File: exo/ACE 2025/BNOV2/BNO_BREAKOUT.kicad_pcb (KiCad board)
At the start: 2 copper layers, 67.5 x 45 mm, 17 parts, among them J2 RJ45, SW1 SW_SPDT, U1 4754, U2 PCA9615DPZ, U3 AP7361C-33E

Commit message: BNOV2 V0.2
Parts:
- removed C4: 4.7uF, Capacitor_SMD:C_1812_4532Metric_Pad1.57x3.40mm_HandSolder
- removed D2: BAV99, Package_TO_SOT_SMD:SOT-23
- added REF**: MountingHole_3.2mm_M3, MountingHole:MountingHole_3.2mm_M3, F.Cu at (121.0, 71.5)
- added REF**: MountingHole_3.2mm_M3, MountingHole:MountingHole_3.2mm_M3, F.Cu at (157.0, 125.5)
- added REF**: MountingHole_3.2mm_M3, MountingHole:MountingHole_3.2mm_M3, F.Cu at (121.0, 125.5)
- added REF**: MountingHole_3.2mm_M3, MountingHole:MountingHole_3.2mm_M3, F.Cu at (157.0, 71.5)
- C2, C3: value 4.7uF -> 1n
- D4: value ESD9B3.3ST5G -> D_TVS_Filled; footprint Diode_SMD:D_SOD-923 -> Diode_SMD:D_0805_2012Metric
- moved J2 36.8 mm to (129.1, 114.0), turned to 0 degrees
- moved U3 36.1 mm to (146.7, 118.7), turned to -90 degrees
- moved SW1 33.9 mm to (129.5, 97.4), turned to -90 degrees
- moved C5 30.9 mm to (151.5, 111.5)
- moved D5 29.6 mm to (149.0, 111.4), turned to 90 degrees
- moved C6 26.1 mm to (144.0, 111.5), turned to 90 degrees
- moved D3 25.5 mm to (146.5, 94.4), turned to 90 degrees
- moved R1 23.7 mm to (146.5, 111.5)
- moved D1 23.6 mm to (139.5, 94.4), turned to 90 degrees
- moved U2 16.1 mm to (134.5, 105.0), turned to -90 degrees
- moved D4 10.7 mm to (150.0, 104.9)
- moved C3 10.6 mm to (139.4, 99.0), turned to 180 degrees
- moved C1 9.64 mm to (145.0, 105.1)
- moved C2 5.08 mm to (146.4, 99.0), turned to 180 degrees
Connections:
- net 5V renamed /5V
- net SCL+ renamed /SCL+
- net SCL- renamed /SCL-
- net SDA+ renamed /SDA+
- net SDA- renamed /SDA-
- C1 pad 1: 3V3 -> /3V3
- C2 pad 1: SDA -> /3V3
- C3 pad 1: SCL -> /3V3
- C6 pad 2: 3V3 -> /3V3
- D1 pad 2: 3V3 -> /3V3
- D1 pad 3: SCL -> /SCL
- D3 pad 2: 3V3 -> /3V3
- D3 pad 3: SDA -> /SDA
- D4 pad 2: 3V3 -> /3V3
- R1 pad 1: 3V3 -> /3V3
- U1 pad JP1_1: 3V3 -> /3V3
- U1 pad JP1_4: SCL -> /SCL
- U1 pad JP1_5: SDA -> /SDA
- U2 pad 1: 3V3 -> /3V3
- U2 pad 2: SDA -> /SDA
- U2 pad 3: 3V3 -> /3V3
- U2 pad 4: SCL -> /SCL
- U3 pad 3: 3V3 -> /3V3
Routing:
- net 3V3: track 73.7 -> 0.00 mm
- net /3V3: track 0.00 -> 71.7 mm
- net GND: track 131.8 -> 82.2 mm, vias 0 -> 10
- net SDA: track 35.2 -> 0.00 mm
- net SCL: track 34.6 -> 0.00 mm
- net Net-(SW1-A): track 33.4 -> 7.64 mm
- net /SDA: track 0.00 -> 24.6 mm
- net /SCL: track 0.00 -> 14.8 mm
- net /5V: track 36.8 -> 26.1 mm
- net /SCL+: track 16.6 -> 7.60 mm
- net /SDA+: track 15.9 -> 6.96 mm
- net Net-(SW1-B): track 40.4 -> 32.4 mm
- net /SDA-: track 13.1 -> 6.85 mm
- net /SCL-: track 13.7 -> 7.56 mm
- net Net-(D5-A): track 4.64 -> 2.50 mm
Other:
- board size 67.5 x 45 mm -> 44 x 62 mm
- board text removed: "DIMENSIONS DELL À CONFIRMER"

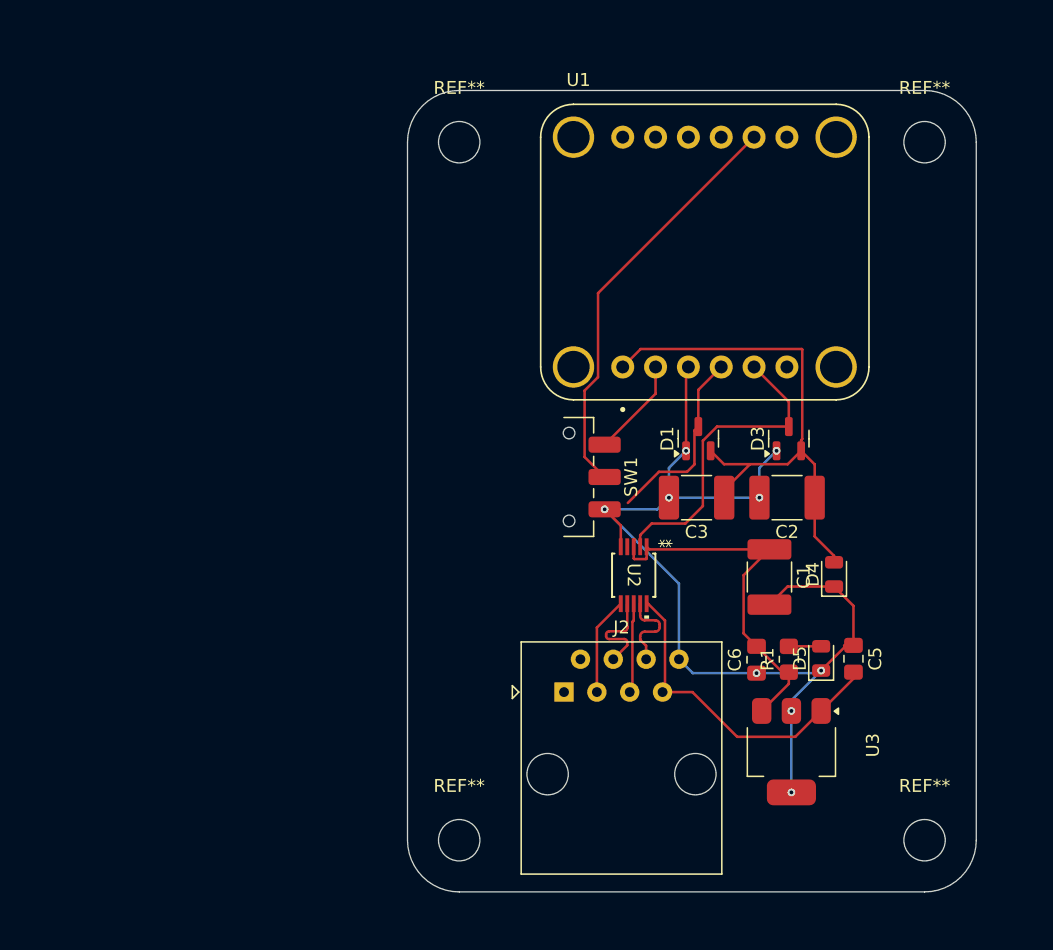
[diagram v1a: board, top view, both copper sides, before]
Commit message: Changement BNO et moustache
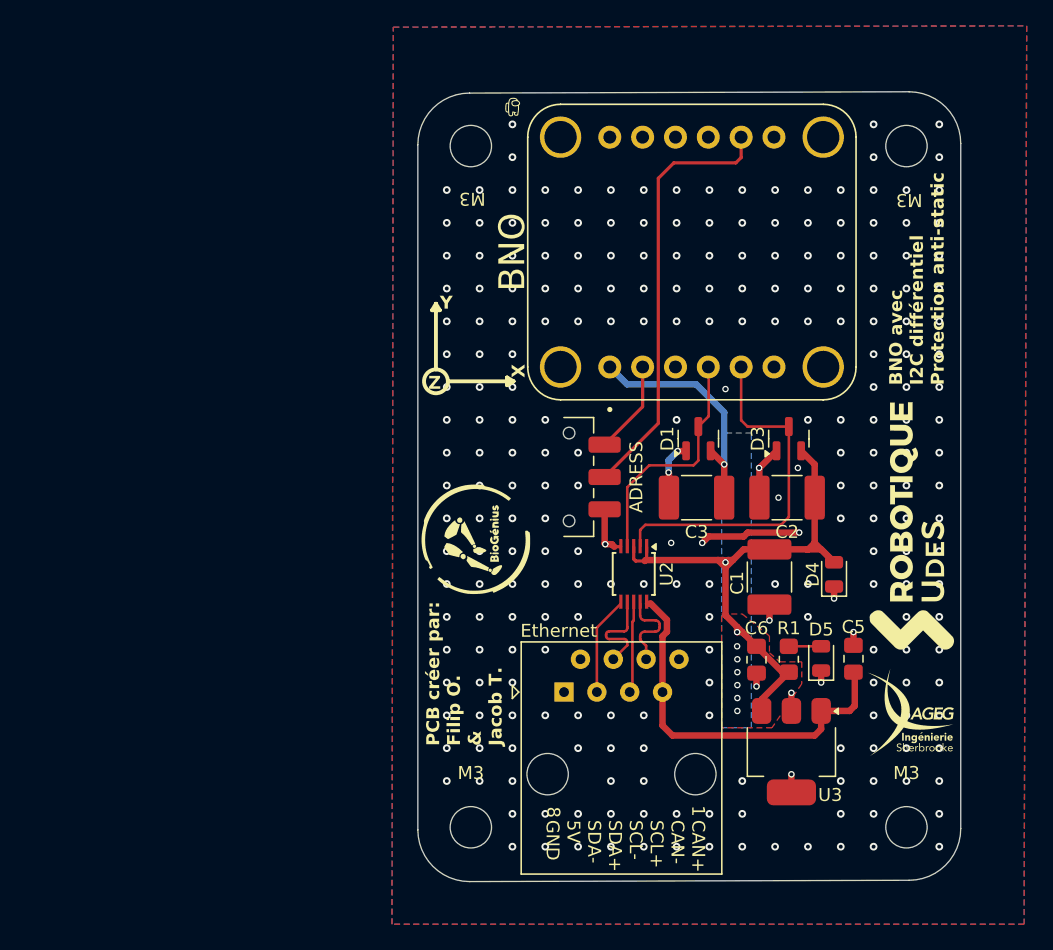
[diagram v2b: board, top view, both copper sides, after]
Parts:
- added G***: LOGO, LOGO, F.Cu at (156.0, 101.3)
- added G***: LOGO, LOGO, F.Cu at (155.9, 115.6)
- U2: footprint Other symbols:TSSOP10_SOT552-1_NXP -> Package_SO:TSSOP-10_3x3mm_P0.5mm
- moved M3 1.72 mm to (155.6, 124.5)
- moved REF** 1.43 mm to (155.6, 71.8)
- moved M3 1.35 mm to (121.9, 124.5)
- moved BNO 1.00 mm to (139.0, 80.0)
- moved REF** 0.95 mm to (121.9, 71.8)
- moved U2 0.10 mm to (134.5, 104.9)
- renumbered SW1 to ADRESS, U1 to BNO, J2 to Ethernet, REF** to M3
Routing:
- net GND: track 82.2 -> 28.6 mm, vias 10 -> 253
- net /3V3: track 71.7 -> 64.2 mm, vias 0 -> 9
- net /5V: track 26.1 -> 29.9 mm
- net /SCL: track 14.8 -> 18.5 mm
- net /SDA: track 24.6 -> 28.2 mm
- net Net-(SW1-B): track 32.4 -> 33.5 mm
- added copper zone on B.Cu, net /3V3
- added copper zone on F.Cu, net /3V3
- added copper zone on B.Cu, net GND
- added copper zone on F.Cu, net GND
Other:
- board size 44 x 62 mm -> 42 x 61.1 mm
- board text added: "1"
- board text added: "8"
- board text added: "BNO avec I2C différentiel Protection anti-static"
- board text added: "CAN+ CAN- SCL+ SCL- SDA+ SDA- 5V GND"
- board text added: "M3"
- board text added: "PAS DE VIS ICI S'IL VOUS PLAÎT"
- board text added: "PCB créer par: Filip O. & Jacob T."
- board text added: "X"
- board text added: "Y"
- board text added: "Z"
